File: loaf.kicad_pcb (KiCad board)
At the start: 2 copper layers, 242.9 x 76.2 mm, 102 parts, among them J1 USB_C_Receptacle_USB2.0, J2 AVR-ISP-6, J3 OLED, SW1 SW_Push, SW10 SW_Push, SW11 SW_Push, SW12 SW_Push, SW13 SW_Push, SW14 SW_Push, SW15 SW_Push, SW16 SW_Push, SW17 SW_Push, SW18 SW_Push, SW19 SW_Push, SW2 SW_Push, SW20 SW_Push, SW21 SW_Push, SW22 SW_Push, SW23 SW_Push, SW24 SW_Push, SW25 SW_Push, SW26 SW_Push, SW27 SW_Push, SW28 SW_Push, SW29 SW_Push, SW3 SW_Push, SW30 SW_Push, SW31 SW_Push, SW32 SW_Push, SW33 SW_Push, SW34 SW_Push, SW35 SW_Push, SW36 SW_Push, SW37 SW_Push, SW38 SW_Push, SW39 SW_Push, SW4 SW_Push, SW5 SW_Push, SW6 SW_Push, SW7 SW_Push, SW8 SW_Push, SW9 SW_Push, U1 ATmega328P-P, Y1 Crystal_Small

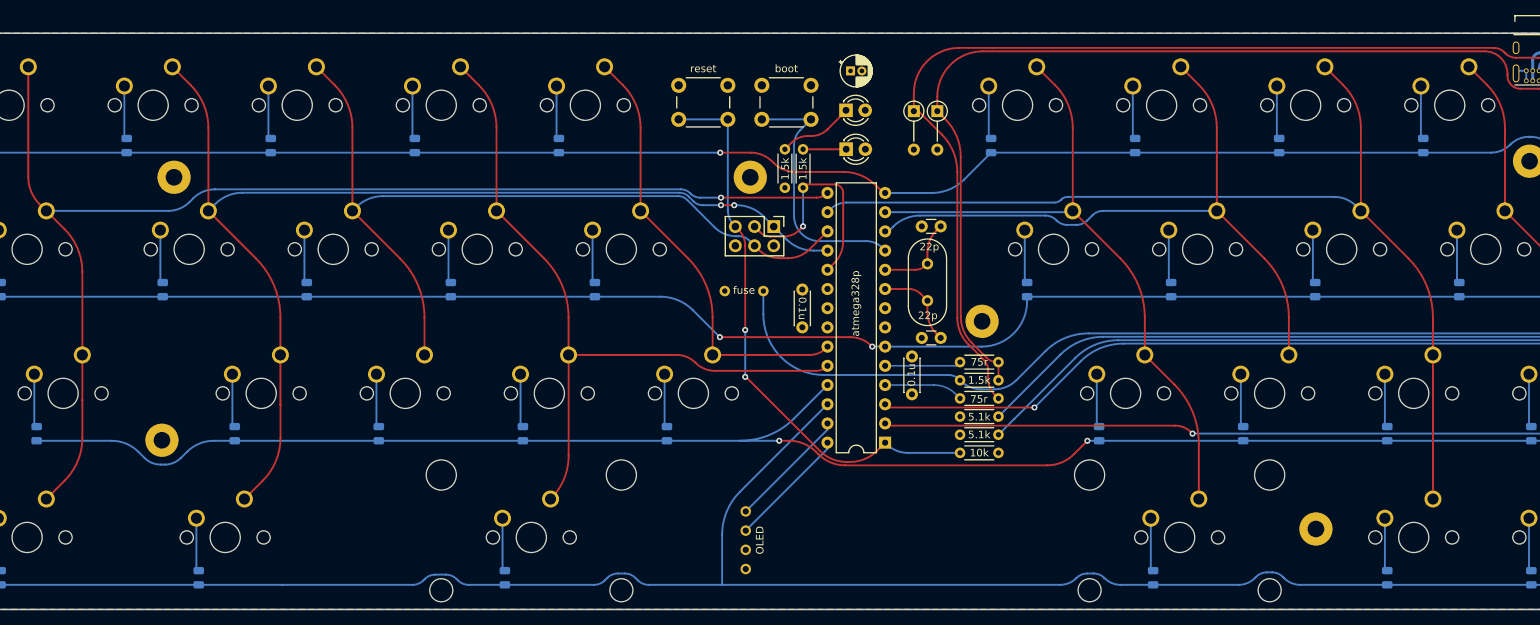
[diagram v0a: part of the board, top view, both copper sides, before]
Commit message: add cover mounting points
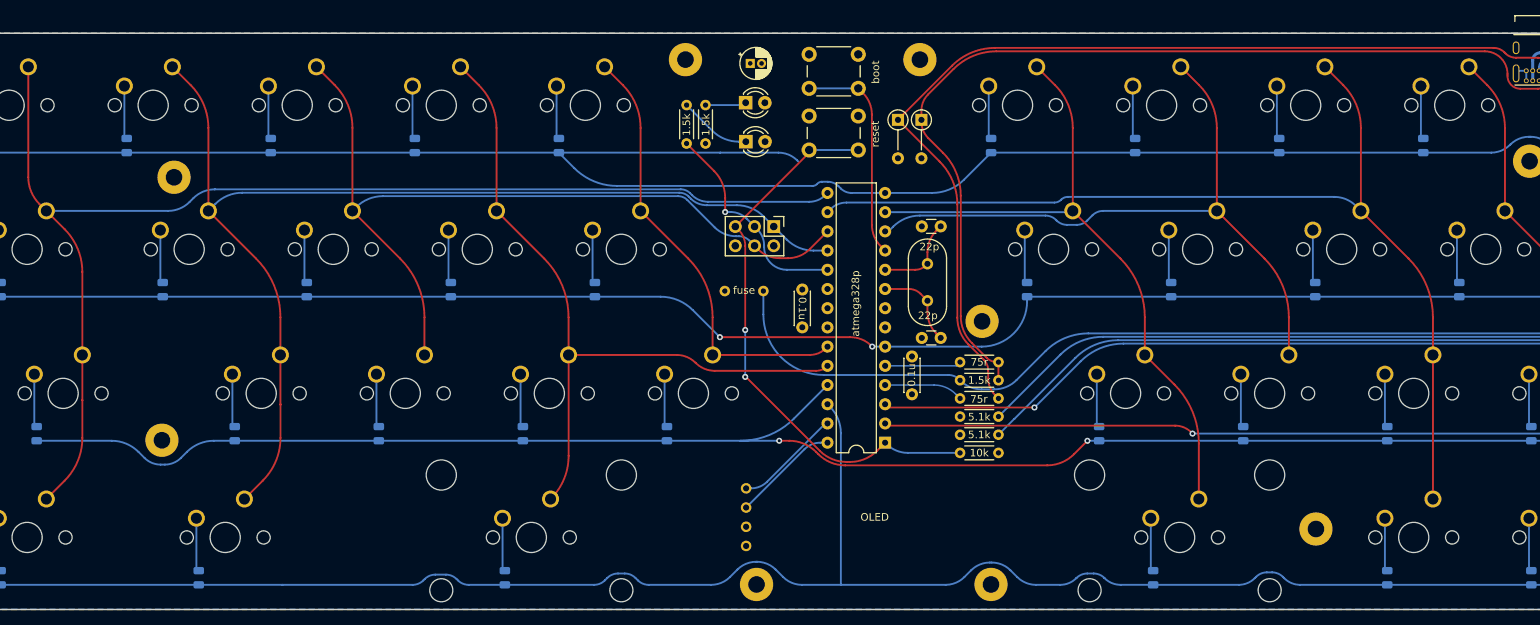
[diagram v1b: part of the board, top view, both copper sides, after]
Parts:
- added REF**: MountingHole_2.2mm_M2_Pad, MountingHole:MountingHole_2.2mm_M2_Pad, F.Cu at (135.3, 129.2)
- added REF**: MountingHole_2.2mm_M2_Pad, MountingHole:MountingHole_2.2mm_M2_Pad, F.Cu at (126.0, 59.9)
- added REF**: MountingHole_2.2mm_M2_Pad, MountingHole:MountingHole_2.2mm_M2_Pad, F.Cu at (156.9, 59.9)
- added REF**: MountingHole_2.2mm_M2_Pad, MountingHole:MountingHole_2.2mm_M2_Pad, F.Cu at (166.3, 129.2)
- moved SW2 17.7 mm to (142.3, 67.3)
- moved R8 16.5 mm to (126.1, 70.9)
- moved D40 13.3 mm to (133.9, 65.5)
- moved C3 13.3 mm to (134.5, 60.4)
- moved D41 13.3 mm to (133.9, 70.7)
- moved R7 12.0 mm to (128.6, 70.9)
- moved SW1 7.47 mm to (142.3, 59.1)
- moved G*** 6.55 mm to (150.8, 125.3)
- moved J3 3.05 mm to (134.0, 120.3)
- moved D1 2.39 mm to (154.1, 67.8)
- moved D2 2.39 mm to (157.2, 67.8)
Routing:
- net ROW0: track 221.2 -> 253.9 mm, vias 1 -> 0
- net BOOT: track 34.2 -> 29.0 mm
- net Net-(D40-Pad1): track 9.97 -> 5.60 mm
- net Net-(D41-Pad1): track 5.70 -> 9.60 mm
- net SCL: track 16.1 -> 14.2 mm
- net SDA: track 16.1 -> 14.2 mm
- net ROW3: track 254.0 -> 252.7 mm
- net Net-(D2-Pad1): track 129.4 -> 130.6 mm
- net SCK/LED: track 29.3 -> 28.5 mm
- net COL0: track 165.6 -> 166.0 mm, vias 1 -> 0
- net MISO/COL1: track 148.9 -> 148.8 mm, vias 2 -> 0

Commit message: fix stray trace
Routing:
- net ROW0: track 253.9 -> 221.8 mm
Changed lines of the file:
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@@
   (segment (start 204.4625 72.14875) (end 223.5125 72.14875) (width 0.25) (layer "B.Cu") (net 7))
   (segment (start 33.0125 72.14875) (end 52.0625 72.14875) (width 0.25) (layer "B.Cu") (net 7))
-  (segment (start 140.924873 73.374873) (end 140.723876 73.173876) (width 0.25) (layer "B.Cu") (net 7))
   (segment (start 142.767669 76.55096) (end 116.914668 76.55096) (width 0.25) (layer "B.Cu") (net 7))
   (segment (start 223.5125 72.14875) (end 232.501503 72.14875) (width 0.25) (layer "B.Cu") (net 7))
   (segment (start 166.3625 72.14875) (end 185.4125 72.14875) (width 0.25) (layer "B.Cu") (net 7))
-  (segment (start 138.249003 72.14875) (end 130.54875 72.14875) (width 0.25) (layer "B.Cu") (net 7))
   (segment (start 71.1125 72.14875) (end 90.1625 72.14875) (width 0.25) (layer "B.Cu") (net 7))
   (segment (start 146.494213 76.894213) (end 146.185786 76.585786) (width 0.25) (layer "B.Cu") (net 7))
   (segment (start 234.976377 71.123623) (end 235.024874 71.075126) (width 0.25) (layer "B.Cu") (net 7))
   (segment (start 152.35 77.48) (end 147.908427 77.48) (width 0.25) (layer "B.Cu") (net 7))
-  (segment (start 130.54875 72.14875) (end 130.55 72.15) (width 0.25) (layer "B.Cu") (net 7))
   (segment (start 144.771573 76) (end 143.981371 76) (width 0.25) (layer "B.Cu") (net 7))
   (segment (start 237.499747 70.05) (end 237.700253 70.05) (width 0.25) (layer "B.Cu") (net 7))
-  (segment (start 109.2125 72.14875) (end 130.54875 72.14875) (width 0.25) (layer "B.Cu") (net 7))
   (segment (start 185.4125 72.14875) (end 204.4625 72.14875) (width 0.25) (layer "B.Cu") (net 7))
   (segment (start 240.175127 71.075127) (end 240.224874 71.124874) (width 0.25) (layer "B.Cu") (net 7))
@@
   (arc (start 144.771573 76) (mid 145.53694 76.152241) (end 146.185786 76.585786) (width 0.25) (layer "B.Cu") (net 7))
   (arc (start 240.224874 71.124874) (mid 241.360355 71.883578) (end 242.699747 72.15) (width 0.25) (layer "B.Cu") (net 7))
-  (arc (start 138.249003 72.14875) (mid 139.588395 72.415172) (end 140.723876 73.173876) (width 0.25) (layer "B.Cu") (net 7))
   (arc (start 143.981371 76) (mid 143.675225 76.060896) (end 143.415686 76.234314) (width 0.25) (layer "B.Cu") (net 7))
   (arc (start 237.499747 70.05) (mid 236.160355 70.316422) (end 235.024874 71.075126) (width 0.25) (layer "B.Cu") (net 7))

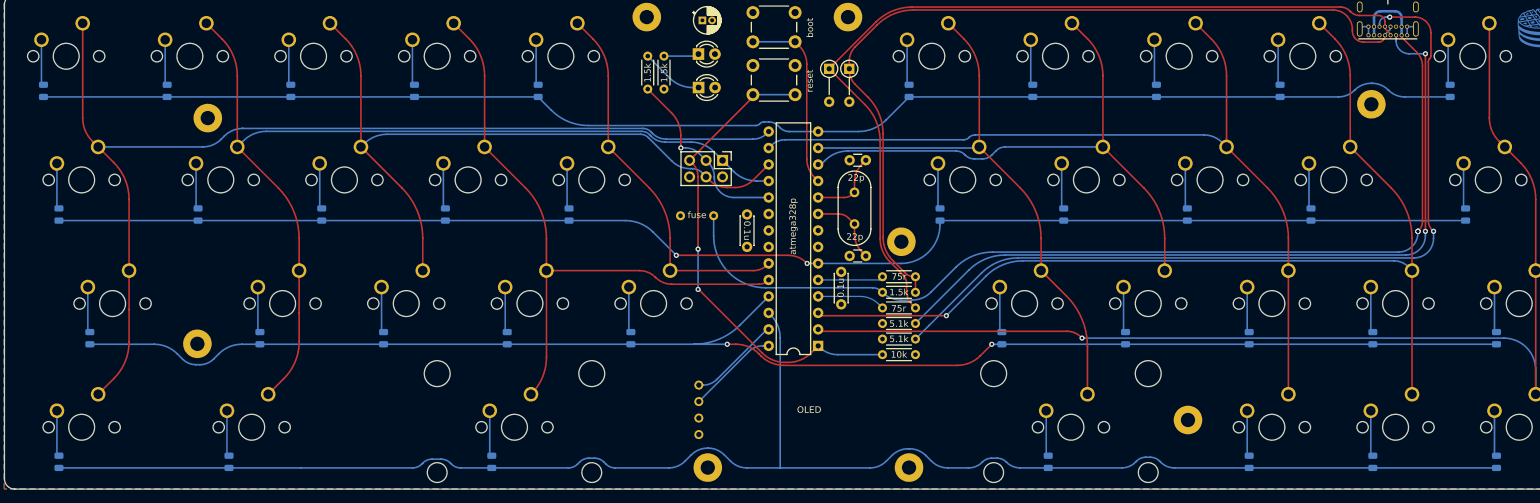
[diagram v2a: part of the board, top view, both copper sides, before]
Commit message: switch diodes to sod-123
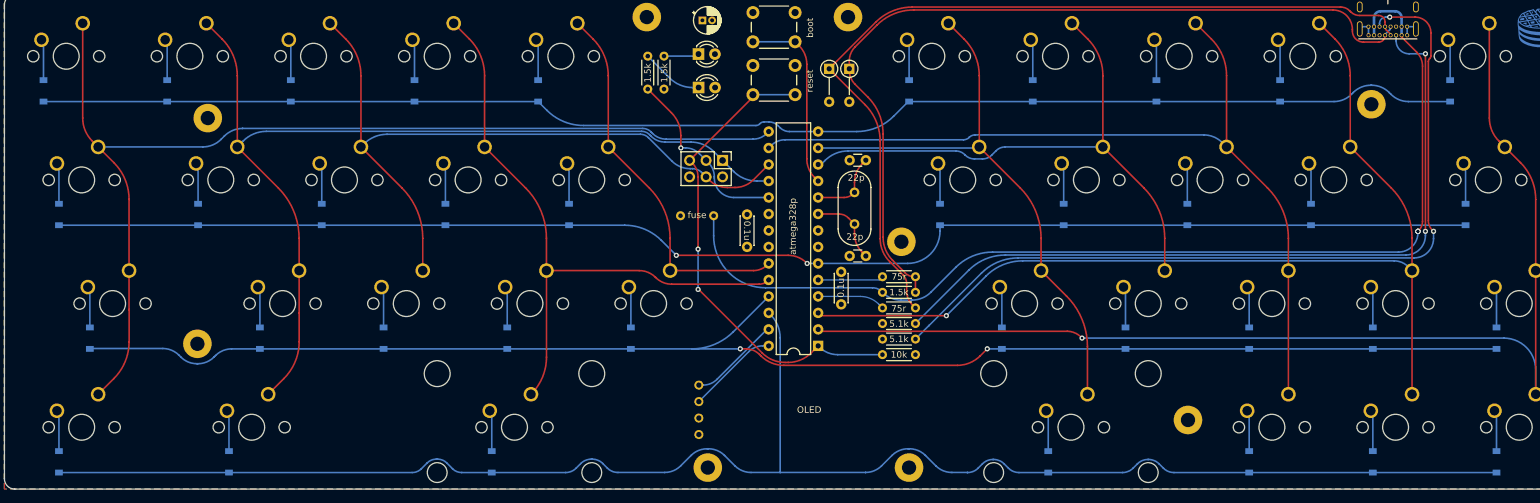
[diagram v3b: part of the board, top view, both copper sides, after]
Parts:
- D10, D11, D12, D13, D14, D15, D16, D17, D18, D19, D20, D21, D22, D23, D24, D25, D26, D27, D28, D29, D3, D30, D31, D32, D33, D34, D35, D36, D37, D38, D39, D4, D5, D6, D7, D8, D9: footprint Diode_SMD:D_0805_2012Metric -> Diode_SMD:D_SOD-123
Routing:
- net ROW3: track 252.7 -> 256.3 mm
- net Net-(D9-Pad2): track 7.06 -> 6.35 mm
- net Net-(D8-Pad2): track 7.06 -> 6.35 mm
- net Net-(D5-Pad2): track 7.06 -> 6.35 mm
- net Net-(D4-Pad2): track 7.06 -> 6.35 mm
- net Net-(D38-Pad2): track 7.06 -> 6.35 mm
- net Net-(D37-Pad2): track 7.06 -> 6.35 mm
- net Net-(D34-Pad2): track 7.06 -> 6.35 mm
- net Net-(D33-Pad2): track 7.06 -> 6.35 mm
- net Net-(D30-Pad2): track 7.06 -> 6.35 mm
- net Net-(D29-Pad2): track 7.06 -> 6.35 mm
- net Net-(D27-Pad2): track 7.06 -> 6.35 mm
- net Net-(D26-Pad2): track 7.06 -> 6.35 mm
- net Net-(D23-Pad2): track 7.06 -> 6.35 mm
- net Net-(D22-Pad2): track 7.06 -> 6.35 mm
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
